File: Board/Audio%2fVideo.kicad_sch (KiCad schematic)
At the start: 10 parts, among them U2 IS61C5128AL-10TLI, X1 SJ1-3513N

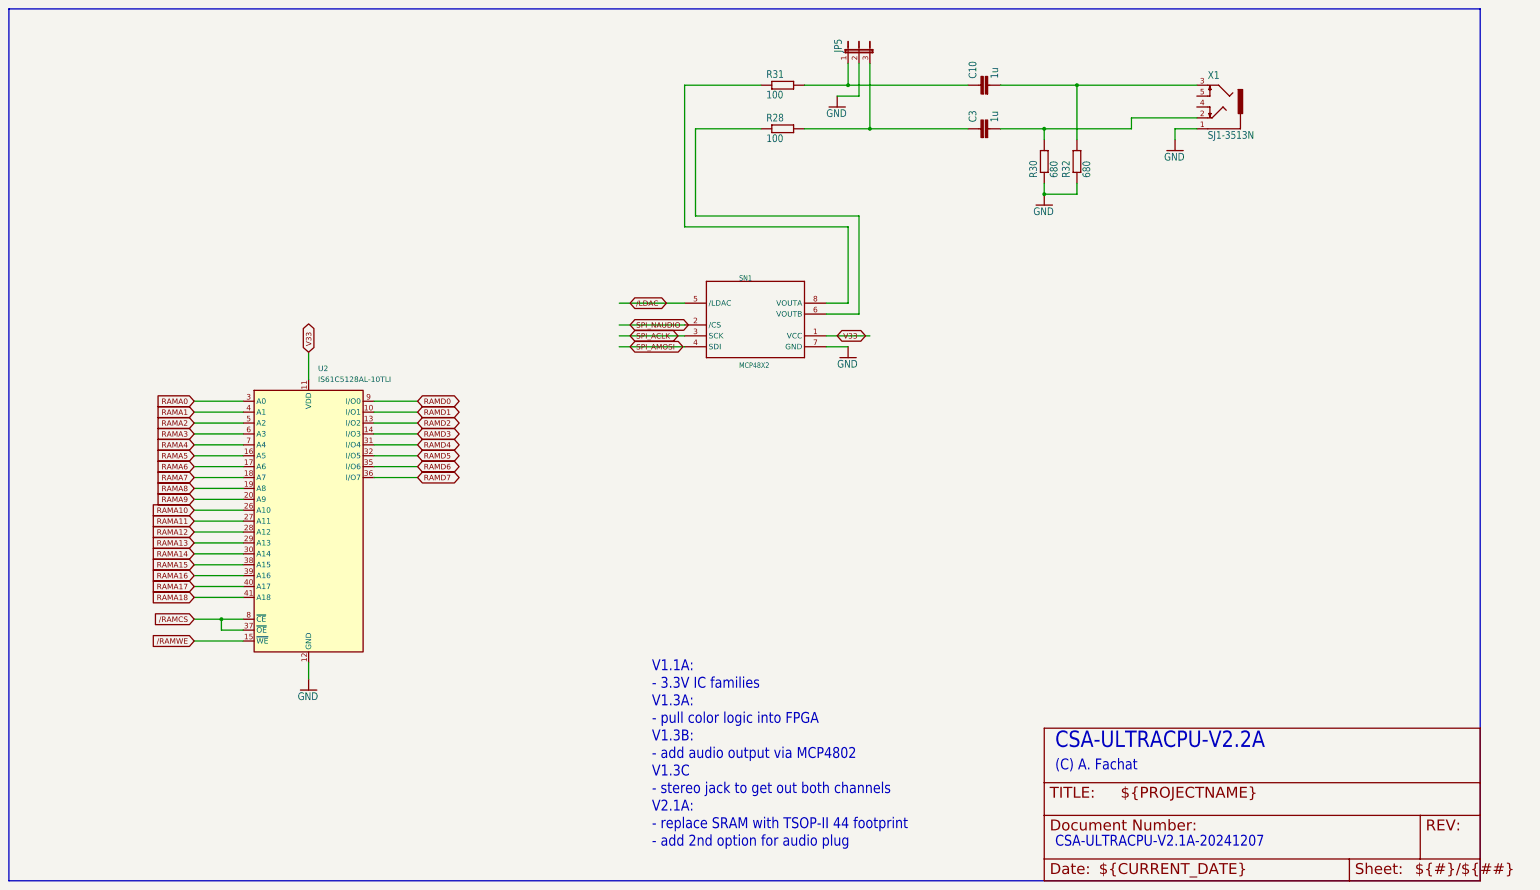
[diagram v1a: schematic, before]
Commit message: start working on 3.0 with larger FPGA
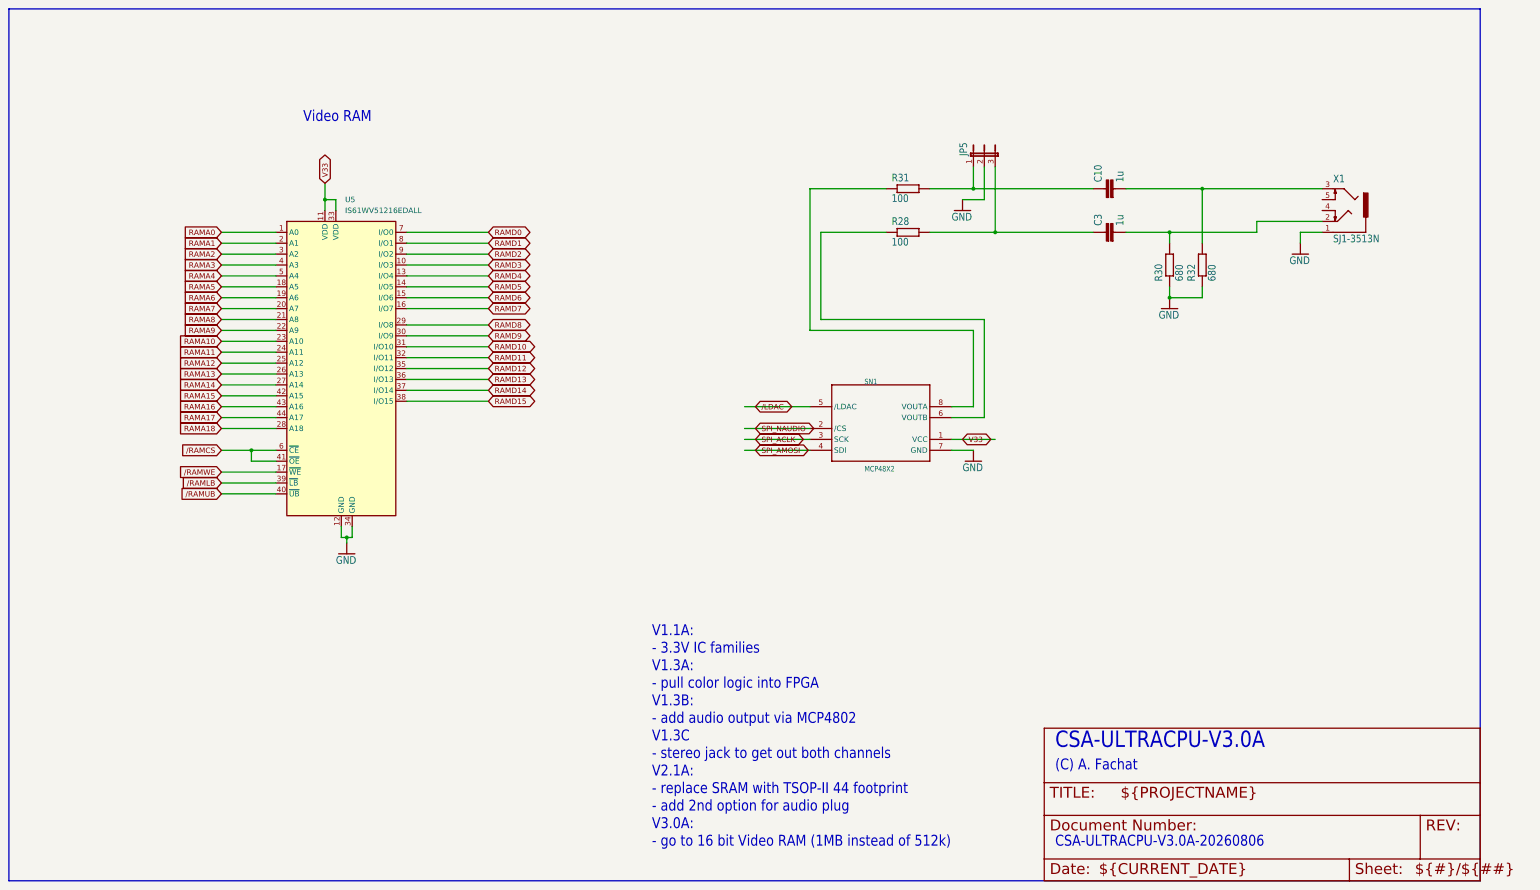
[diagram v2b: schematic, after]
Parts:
- removed U2: IS61C5128AL-10TLI, Package_SO:TSOP-II-44_10.16x18.41mm_P0.8mm, symbol Memory_RAM:IS61C5128AL-10TLI
- added U5: IS61WV51216EDALL, Package_SO:TSOP-II-44_10.16x18.41mm_P0.8mm, symbol csa_ultracpu-eagle-import:IS61WV51216EDALL
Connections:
- net GND: now also U5.12 (GND), U5.34 (GND)
- net RAMA0: now also U5.1 (A0)
- net RAMA1: now also U5.2 (A1)
- net RAMA10: now also U5.23 (A10)
- net RAMA11: now also U5.24 (A11)
- net RAMA12: now also U5.25 (A12)
- net RAMA13: now also U5.26 (A13)
- net RAMA14: now also U5.27 (A14)
- net RAMA15: now also U5.42 (A15)
- net RAMA16: now also U5.43 (A16)
- net RAMA17: now also U5.44 (A17)
- net RAMA18: now also U5.28 (A18)
- net RAMA2: now also U5.3 (A2)
- net RAMA3: now also U5.4 (A3)
- net RAMA4: now also U5.5 (A4)
- net RAMA5: now also U5.18 (A5)
- net RAMA6: now also U5.19 (A6)
- net RAMA7: now also U5.20 (A7)
- net RAMA8: now also U5.21 (A8)
- net RAMA9: now also U5.22 (A9)
- net RAMD0: now also U5.7 (I/O0)
- net RAMD1: now also U5.8 (I/O1)
- net RAMD2: now also U5.9 (I/O2)
- net RAMD3: now also U5.10 (I/O3)
- net RAMD4: now also U5.13 (I/O4)
- net RAMD5: now also U5.14 (I/O5)
- net RAMD6: now also U5.15 (I/O6)
- net RAMD7: now also U5.16 (I/O7)
- net V33: now also U5.11 (VDD), U5.33 (VDD)
- net /RAMCS: now also U5.41 (~{OE}), U5.6 (~{CE})
- net /RAMWE: now also U5.17 (~{WE})
- new net RAMD10: U5.31 (I/O10)
- new net RAMD11: U5.32 (I/O11)
- new net RAMD12: U5.35 (I/O12)
- new net RAMD13: U5.36 (I/O13)
- new net RAMD14: U5.37 (I/O14)
- new net RAMD15: U5.38 (I/O15)
- new net RAMD8: U5.29 (I/O8)
- new net RAMD9: U5.30 (I/O9)
- new net /RAMLB: U5.39 (~{LB})
- new net /RAMUB: U5.40 (~{UB})
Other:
- note added: "CSA-ULTRACPU-V3.0A"
- note added: "CSA-ULTRACPU-V3.0A-20260806"
- note added: "V1.1A: - 3.3V IC families V1.3A: - pull color logic into FPGA V1.3B: - add audio output via MCP4802 V1.3C - stereo jack to get out both channels V2.1A: - replace SRAM with TSOP-II 44 footprint - add 2nd option for audio plug V3.0A: - go to 16 bit Video RAM (1MB instead of 512k)"
- note added: "Video RAM"
- note removed: "CSA-ULTRACPU-V2.1A-20241207"
- note removed: "CSA-ULTRACPU-V2.2A"
- note removed: "V1.1A: - 3.3V IC families V1.3A: - pull color logic into FPGA V1.3B: - add audio output via MCP4802 V1.3C - stereo jack to get out both channels V2.1A: - replace SRAM with TSOP-II 44 footprint - add 2nd option for audio plug"
- moved on the sheet: C10, C3, JP5, R28, R30, R31, R32, SN1, X1

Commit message: layout done
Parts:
- C10, C3: footprint csa_ultracpu:C050-025X075 -> Capacitor_SMD:C_0603_1608Metric; LCSC (none) -> C15849
- JP5: LCSC (none) -> C587036
- R28, R31: footprint csa_ultracpu:0204V -> Resistor_SMD:R_0603_1608Metric_Pad0.98x0.95mm_HandSolder; LCSC (none) -> C22775
- R30, R32: footprint csa_ultracpu:0204V -> Resistor_SMD:R_0603_1608Metric_Pad0.98x0.95mm_HandSolder; LCSC (none) -> C23228
- SN1: LCSC (none) -> C144363
- U5: LCSC (none) -> C57407
- X1: LCSC (none) -> C145814
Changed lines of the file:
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@@
+			)
+		)
+		(property "LCSC" "C144363"
+			(at 217.17 105.41 0)
+			(hide yes)
+			(show_name no)
+			(do_not_autoplace no)
+			(effects
+				(font
+					(size 1.27 1.27)
+				)
 			)
 		)
@@
 			)
 		)
-		(property "Footprint" "csa_ultracpu:C050-025X075"
+		(property "Footprint" "Capacitor_SMD:C_0603_1608Metric"
 			(at 273.05 59.69 0)
 			(hide yes)
@@
 		(property "Description" ""
 			(at 273.05 59.69 0)
+			(hide yes)
+			(show_name no)
+			(do_not_autoplace no)
+			(effects
+				(font
+					(size 1.27 1.27)
+				)
+			)
+		)
+		(property "LCSC" "C15849"
+			(at 272.669 58.166 0)
 			(hide yes)
 			(show_name no)
@@
 			)
 		)
+		(property "LCSC" "C145814"
+			(at 326.39 58.42 0)
+			(hide yes)
+			(show_name no)
+			(do_not_autoplace no)
+			(effects
+				(font
+					(size 1.27 1.27)
+				)
+			)
+		)
 		(pin "1"
 		)
@@
 			)
 		)
-		(property "Footprint" "csa_ultracpu:0204V"
+		(property "Footprint" "Resistor_SMD:R_0603_1608Metric_Pad0.98x0.95mm_HandSolder"
 			(at 295.91 77.47 0)
 			(hide yes)
@@
 		(property "Description" ""
 			(at 295.91 77.47 0)
+			(hide yes)
+			(show_name no)
+			(do_not_autoplace no)
+			(effects
+				(font
+					(size 1.27 1.27)
+				)
+			)
+		)
+		(property "LCSC" "C23228"
+			(at 294.4114 81.28 0)
 			(hide yes)
 			(show_name no)
@@
 			)
 		)
-		(property "Footprint" "csa_ultracpu:0204V"
+		(property "Footprint" "Resistor_SMD:R_0603_1608Metric_Pad0.98x0.95mm_HandSolder"
 			(at 288.29 77.47 0)
 			(hide yes)
@@
 		(property "Description" ""
 			(at 288.29 77.47 0)
+			(hide yes)
+			(show_name no)
+			(do_not_autoplace no)
+			(effects
+				(font
+					(size 1.27 1.27)
+				)
+			)
+		)
+		(property "LCSC" "C23228"
+			(at 286.7914 81.28 0)
 			(hide yes)
 			(show_name no)
@@
 			)
 		)
+		(property "LCSC" "C587036"
+			(at 241.3 52.07 0)
+			(hide yes)
+			(show_name no)
+			(do_not_autoplace no)
+			(effects
+				(font
+					(size 1.27 1.27)
+				)
+			)
+		)
 		(pin "1"
 		)
@@
 			)
 		)
-		(property "Footprint" "csa_ultracpu:0204V"
+		(property "Footprint" "Resistor_SMD:R_0603_1608Metric_Pad0.98x0.95mm_HandSolder"
 			(at 227.33 59.69 0)
 			(hide yes)
@@
 		(property "Description" ""
 			(at 227.33 59.69 0)
+			(hide yes)
+			(show_name no)
+			(do_not_autoplace no)
+			(effects
+				(font
+					(size 1.27 1.27)
+				)
+			)
+		)
+		(property "LCSC" "C22775"
+			(at 223.52 58.1914 0)
 			(hide yes)
 			(show_name no)
@@
 			)
 		)
-		(property "Footprint" "csa_ultracpu:C050-025X075"
+		(property "Footprint" "Capacitor_SMD:C_0603_1608Metric"
 			(at 273.05 69.85 0)
 			(hide yes)
@@
 		(property "Description" ""
 			(at 273.05 69.85 0)
+			(hide yes)
+			(show_name no)
+			(do_not_autoplace no)
+			(effects
+				(font
+					(size 1.27 1.27)
+				)
+			)
+		)
+		(property "LCSC" "C15849"
+			(at 272.669 68.326 0)
 			(hide yes)
 			(show_name no)
@@
 			)
 		)
+		(property "LCSC" "C57407"
+			(at 96.1233 62.23 0)
+			(hide yes)
+			(show_name no)
+			(do_not_autoplace no)
+			(effects
+				(font
+					(size 1.27 1.27)
+				)
+			)
+		)
 		(pin "44"
 		)
@@
 			)
 		)
-		(property "Footprint" "csa_ultracpu:0204V"
+		(property "Footprint" "Resistor_SMD:R_0603_1608Metric_Pad0.98x0.95mm_HandSolder"
 			(at 227.33 69.85 0)
 			(hide yes)
@@
 			(hide yes)
 			(show_name no)
+			(do_not_autoplace no)
+			(effects
+				(font
+					(size 1.27 1.27)
+				)
+			)
+		)
+		(property "LCSC" "C22775"
+			(at 223.52 68.3514 0)
+			(hide yes)
+			(show_name no)
